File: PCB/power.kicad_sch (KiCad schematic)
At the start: 7 parts, among them U6 TPS61023DRLR

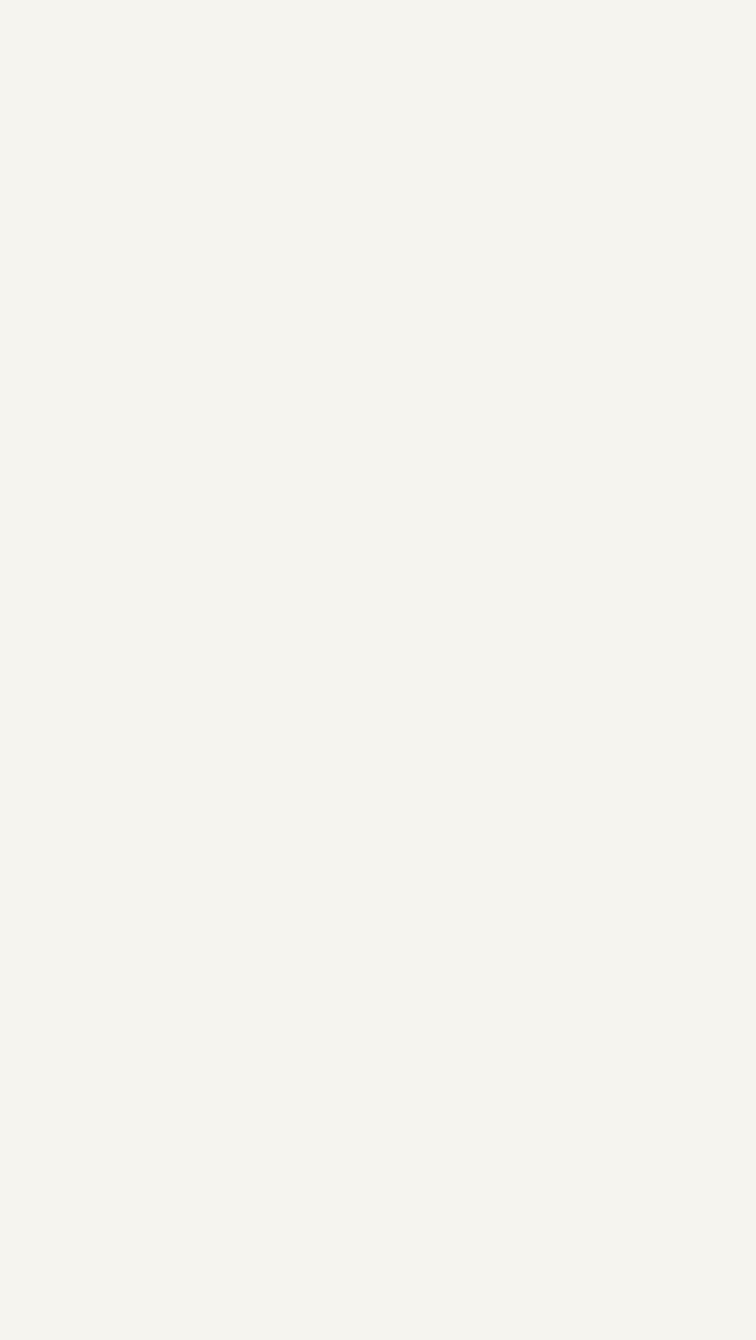
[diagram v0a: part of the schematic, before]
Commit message: volt reg to power page
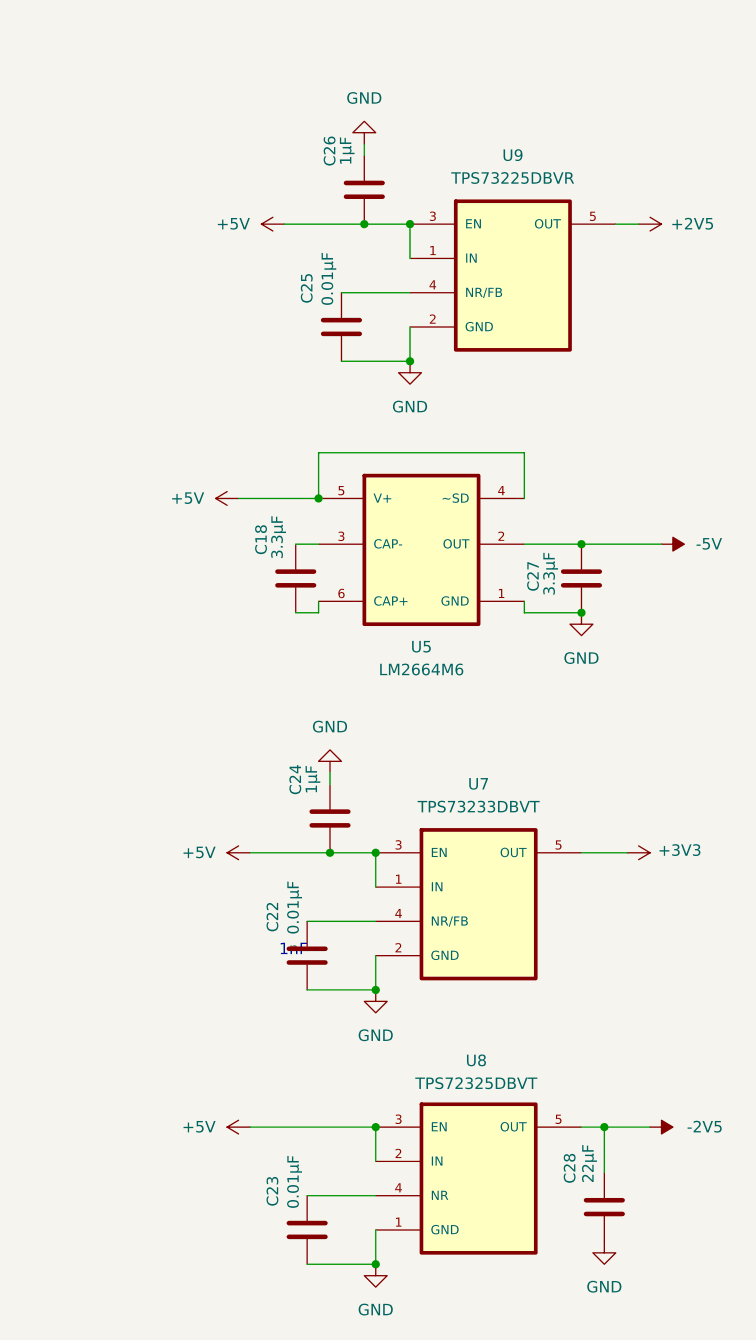
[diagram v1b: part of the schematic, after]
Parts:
- added C18, C27: 3.3µF, symbol Device:C
- added C22, C23, C25: 0.01µF, symbol Device:C
- added C24, C26: 1µF, symbol Device:C
- added C28: 22µF, symbol Device:C
- added U5: LM2664M6, LM2664M6:SOT95P300X120-6N, symbol custom_lib:LM2664M6
- added U7: TPS73233DBVT, TPS73233DBVT:SOT95P280X145-5N, symbol custom_lib:TPS73233DBVT
- added U8: TPS72325DBVT, TPS72325DBVT:SOT95P280X145-5N, symbol custom_lib:TPS72325DBVT
- added U9: TPS73225DBVR, TPS73225DBVR:SOT95P280X145-5N, symbol custom_lib:TPS73225DBVR
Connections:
- net +5V: now also C24.1, C26.1, U5.4 (~SD), U5.5 (V+), U7.1 (IN), U7.3 (EN), U8.2 (IN), U8.3 (EN), U9.1 (IN), U9.3 (EN)
- net GND: now also C22.1, C23.1, C24.2, C25.1, C26.2, C27.1, C28.1, U5.1 (GND), U7.2 (GND), U8.1 (GND), U9.2 (GND)
- new net: C22.2, U7.4 (NR/FB)
- new net: C18.2, U5.3 (CAP-)
- new net: C18.1, U5.6 (CAP+)
- new net: C25.2, U9.4 (NR/FB)
- new net: C23.2, U8.4 (NR)
- new net +2V5: U9.5 (OUT)
- new net +3V3: U7.5 (OUT)
- new net -2V5: C28.2, U8.5 (OUT)
- new net -5V: C27.2, U5.2 (OUT)
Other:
- note added: "1nF"

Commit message: other pages for volt regs
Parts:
- removed C18, C27: 3.3µF, symbol Device:C
- removed C22, C23, C25: 0.01µF, symbol Device:C
- removed C24, C26: 1µF, symbol Device:C
- removed C28: 22µF, symbol Device:C
- removed U5: LM2664M6, LM2664M6:SOT95P300X120-6N, symbol custom_lib:LM2664M6
- removed U7: TPS73233DBVT, TPS73233DBVT:SOT95P280X145-5N, symbol custom_lib:TPS73233DBVT
- removed U8: TPS72325DBVT, TPS72325DBVT:SOT95P280X145-5N, symbol custom_lib:TPS72325DBVT
- removed U9: TPS73225DBVR, TPS73225DBVR:SOT95P280X145-5N, symbol custom_lib:TPS73225DBVR
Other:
- note added: "Battery boost converter 2.7V to 4.35V input 5V @ 1.5A output"
- note removed: "1nF"
- note removed: "Battery boost converter 2V to 4.2V input 5V @ 2A output"
- moved on the sheet: C19, C20, C21, L1, R4, R5, U6
